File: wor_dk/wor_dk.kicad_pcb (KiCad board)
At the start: 4 copper layers, 135 parts, among them J101 Conn_01x02, J102 Conn_02x03_Odd_Even, J103 Conn_02x03_Odd_Even, J104 Conn_01x02, J201 SWD, J301 SMA, J302 Conn_02x04_Odd_Even, J303 Conn_02x06_Odd_Even, J401 USB_C_Receptacle_USB2.0_16P, J501 SWD, J502 USB_C_Receptacle_USB2.0_16P, J503 SWD, Q501 BSS84, SW201 SW_Push, SW501 SW_Push, U201 nRF52840, U202 TMUX1112PWR, U203 TMUX1112PWR, U301 Si4467, U401 FT232RL, U501 TLV1117-33, U502 LPC11U35FHI33_501, Y201 32.768kHz, Y202 32MHz, Y301 26MHz, Y501 12MHz

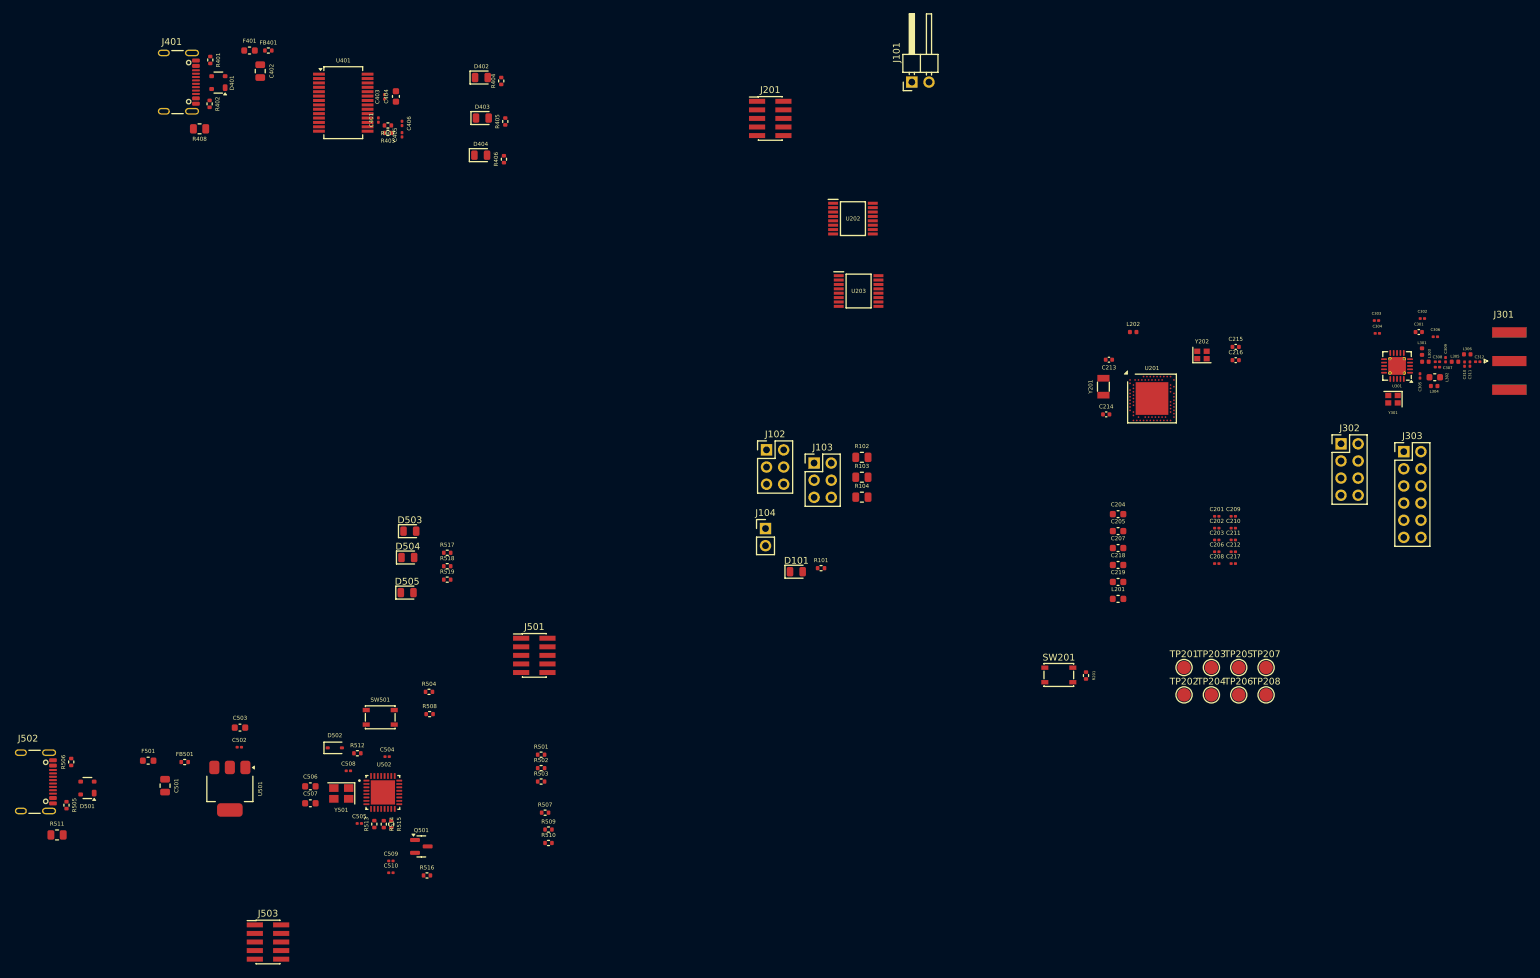
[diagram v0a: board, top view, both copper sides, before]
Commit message: wor_dk: PCB: finer parts placement & interface description
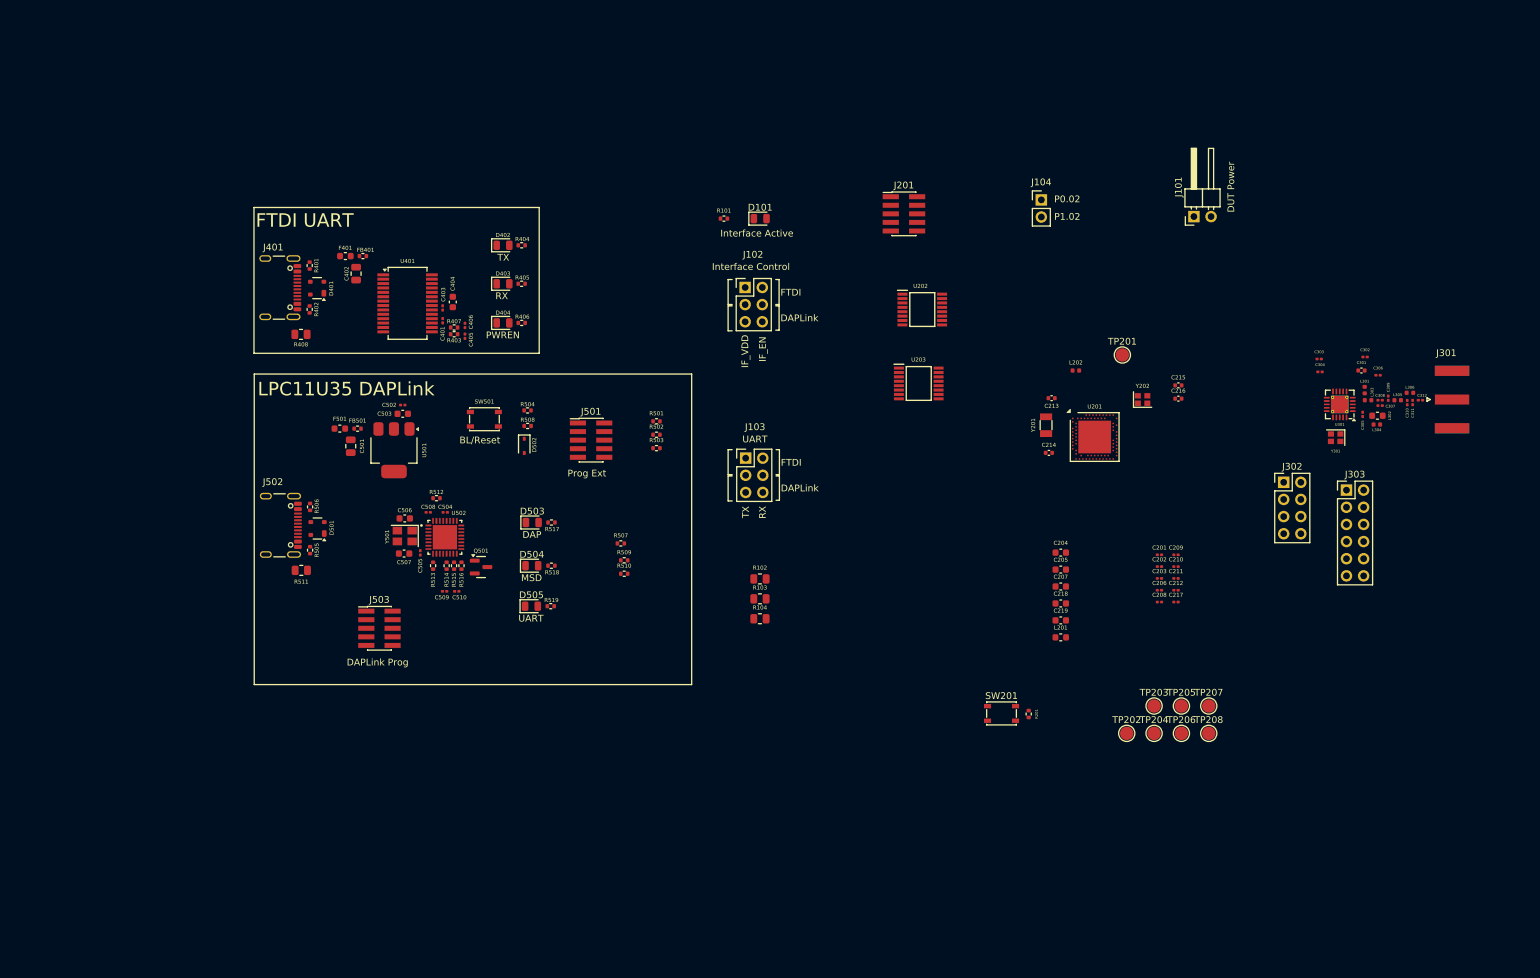
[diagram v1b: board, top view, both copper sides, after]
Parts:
- moved J104 63.6 mm to (172.8, 54.1)
- moved C501 57.3 mm to (70.5, 90.6)
- moved F501 56.8 mm to (68.9, 88.0)
- moved C502 56.2 mm to (78.2, 84.5)
- moved U501 55.7 mm to (76.9, 91.2)
- moved FB501 55.6 mm to (71.5, 88.0)
- moved R101 53.7 mm to (125.8, 56.9)
- moved R511 53.3 mm to (63.2, 109.0)
- moved D502 52.8 mm to (96.2, 90.6), turned to -90 degrees
- moved D101 52.6 mm to (131.2, 56.9)
- moved J502 52.5 mm to (59.0, 102.3)
- moved C503 52.4 mm to (78.2, 85.8)
- moved R501 52.3 mm to (115.8, 86.9)
- moved R502 52.3 mm to (115.8, 88.9)
- moved R503 52.3 mm to (115.8, 90.9)
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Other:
- board text added: "BL/Reset"
- board text added: "DAP"
- board text added: "DAPLink"
- board text added: "DAPLink Prog"
- board text added: "DUT Power"
- board text added: "FTDI"
- board text added: "FTDI UART"
- board text added: "IF_EN"
- board text added: "IF_VDD"
- board text added: "Interface Active"
- board text added: "Interface Control"
- board text added: "LPC11U35 DAPLink"
- board text added: "MSD"
- board text added: "P0.02"
- board text added: "P1.02"
- board text added: "PWREN"
- board text added: "Prog Ext"
- board text added: "RX"
- board text added: "TX"
- board text added: "UART"

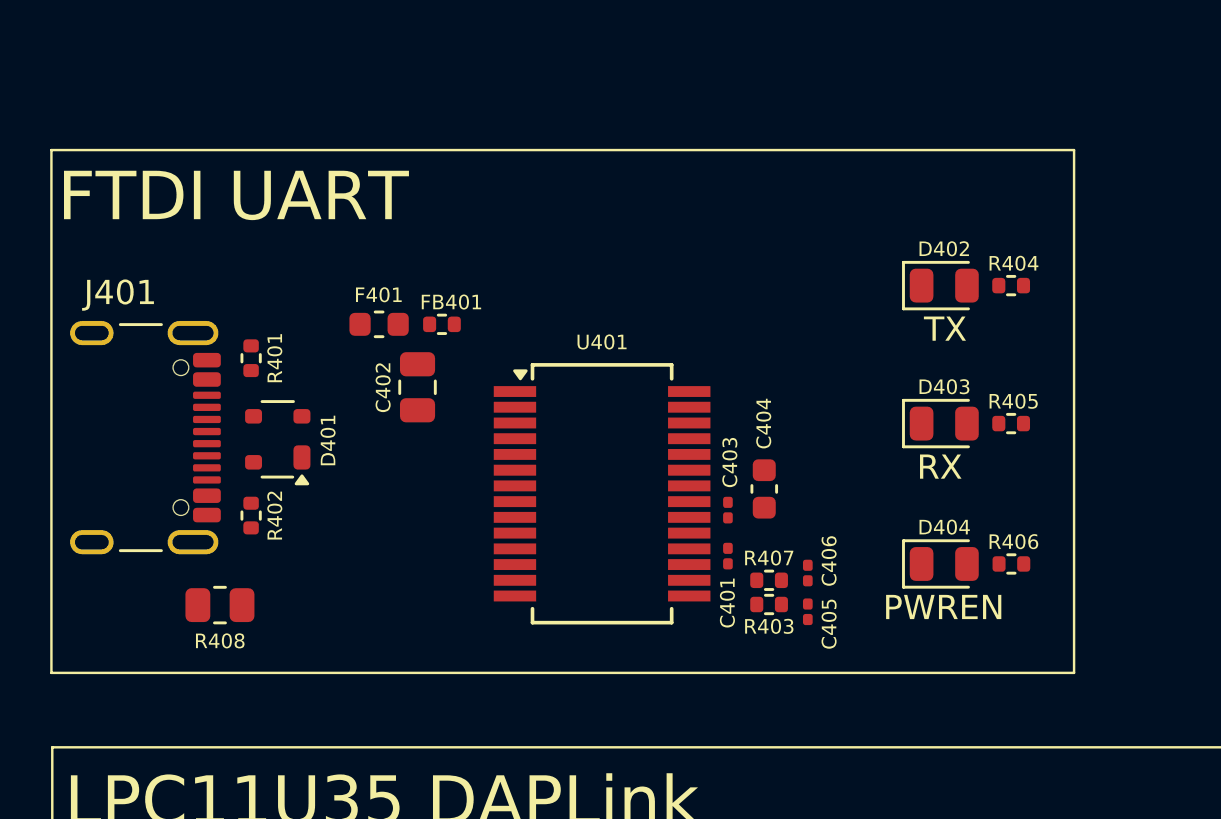
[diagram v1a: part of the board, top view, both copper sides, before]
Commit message: wor_dk: PCB: routing for FTDI part
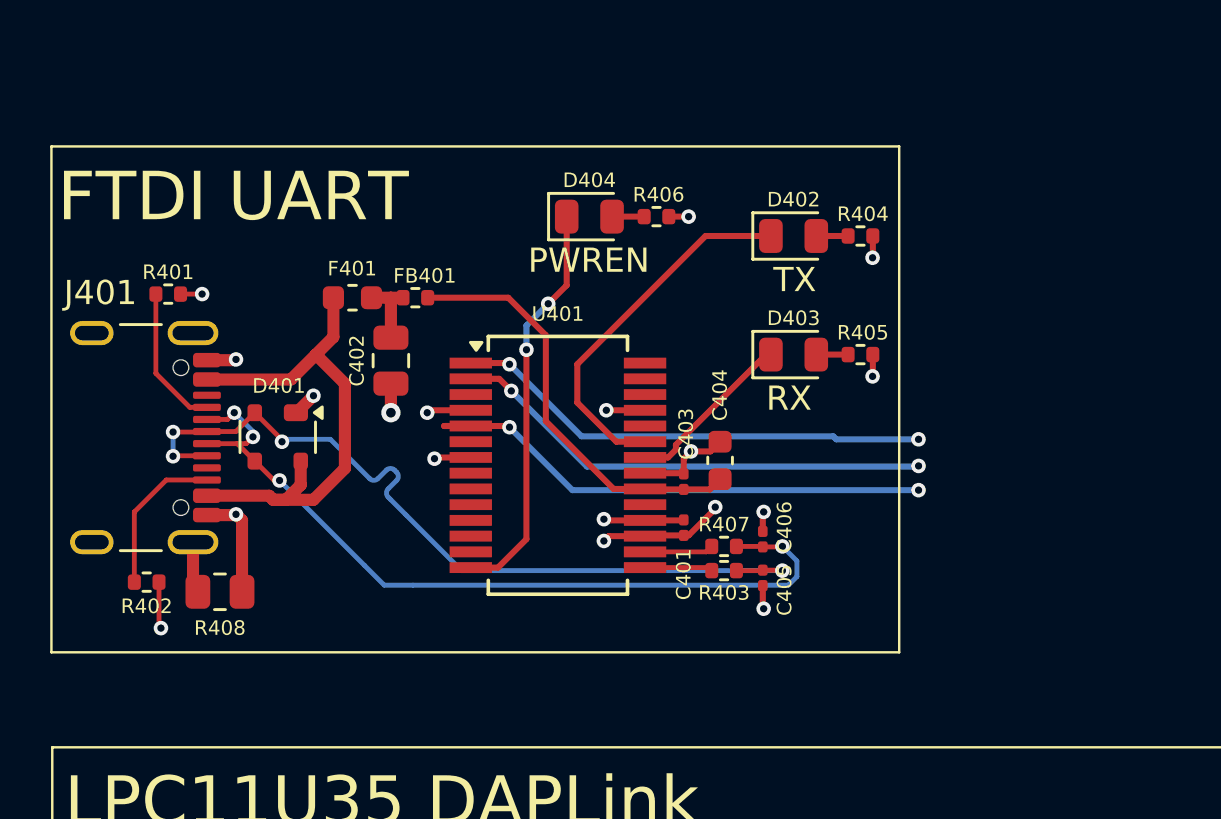
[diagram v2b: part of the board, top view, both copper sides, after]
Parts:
- moved D404 20.5 mm to (78.4, 58.0)
- moved R406 20.5 mm to (81.2, 58.0)
- moved R405 6.85 mm to (89.6, 63.7)
- moved D403 6.85 mm to (86.8, 63.7)
- moved R404 6.55 mm to (89.6, 58.8)
- moved D402 6.55 mm to (86.8, 58.8)
- moved R402 5.12 mm to (60.1, 73.1), turned to 0 degrees
- moved R401 4.33 mm to (61.0, 61.2), turned to 180 degrees
- moved C405 2.33 mm to (85.6, 72.9)
- moved R403 2.33 mm to (84.0, 72.6)
- moved R407 2.33 mm to (84.0, 71.6)
- moved C406 2.33 mm to (85.6, 71.3)
- moved C401 2.17 mm to (82.3, 70.8)
- moved C403 2.17 mm to (82.3, 69.0)
- moved C404 2.17 mm to (83.8, 68.1)
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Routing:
- net /FT232R/USB_D+: track 0.00 -> 34.2 mm, vias 0 -> 4
- net /FT232R/USB_D-: track 0.00 -> 33.7 mm, vias 0 -> 4
- net GND: track 0.00 -> 23.0 mm, vias 0 -> 12
- net /RXD_FTDI: track 0.00 -> 21.8 mm, vias 0 -> 2
- net /FT232R/VBUS: track 0.00 -> 21.5 mm
- net /DTR_FTDI: track 0.00 -> 20.0 mm, vias 0 -> 2
- net /TXD_FTDI: track 0.00 -> 19.8 mm, vias 0 -> 2
- net Net-(U401-VCC): track 0.00 -> 17.6 mm
- net Net-(D404-K): track 0.00 -> 16.8 mm, vias 0 -> 2
- net Net-(D402-K): track 0.00 -> 15.2 mm
- net /3V3_FTDI: track 0.00 -> 9.69 mm, vias 0 -> 6
- net Net-(D403-K): track 0.00 -> 7.08 mm
- net Net-(J401-CC2): track 0.00 -> 6.45 mm
- net Net-(J401-CC1): track 0.00 -> 5.97 mm
- net Net-(C402-Pad1): track 0.00 -> 2.95 mm
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- added copper zone on In2.Cu, net /3V3_FTDI
- added copper zone on In1.Cu, net GND

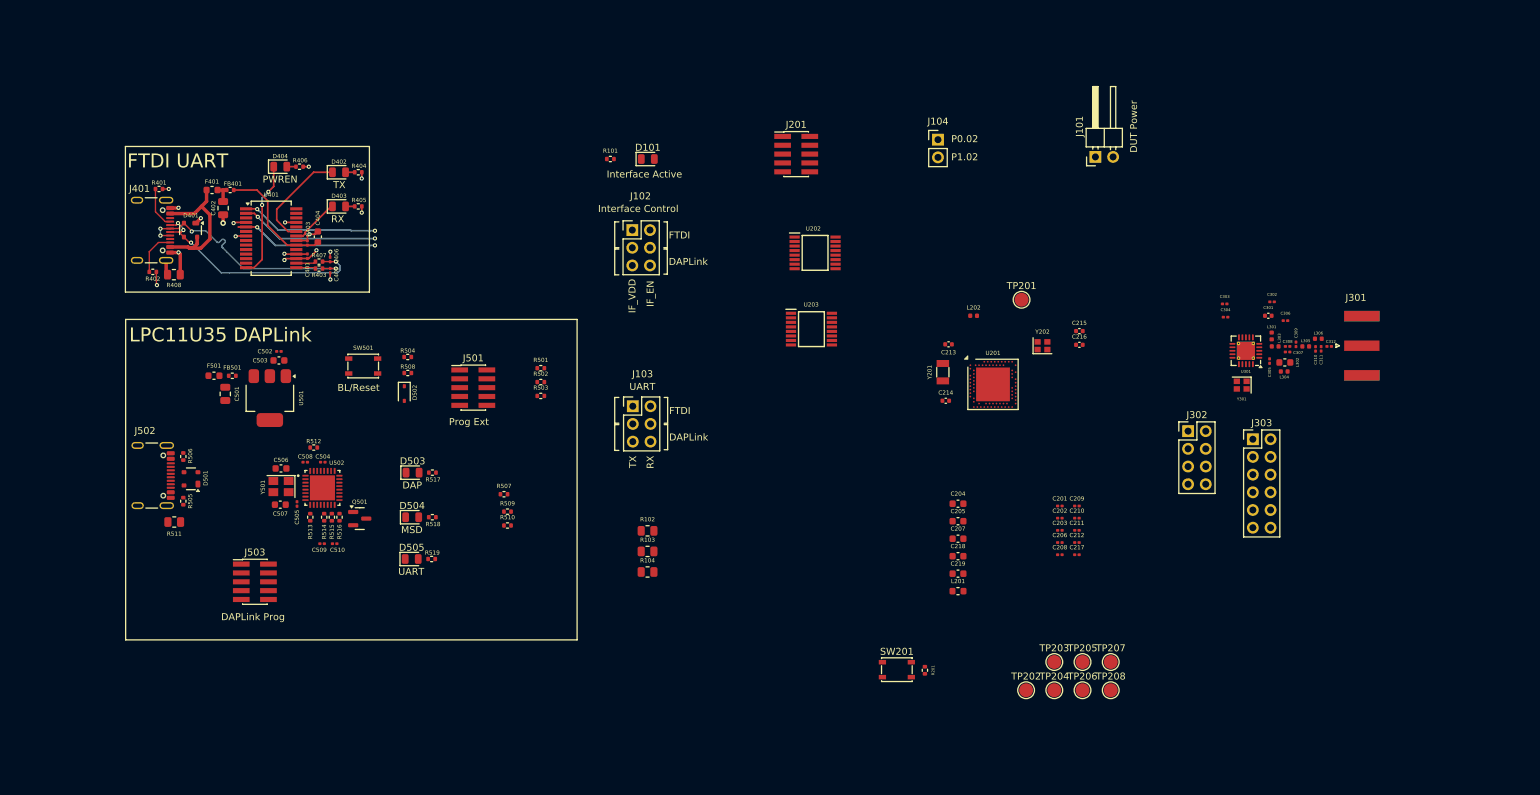
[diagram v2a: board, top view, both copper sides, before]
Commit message: wor_dk: PCB: routing for LPC11U35 DAPLink
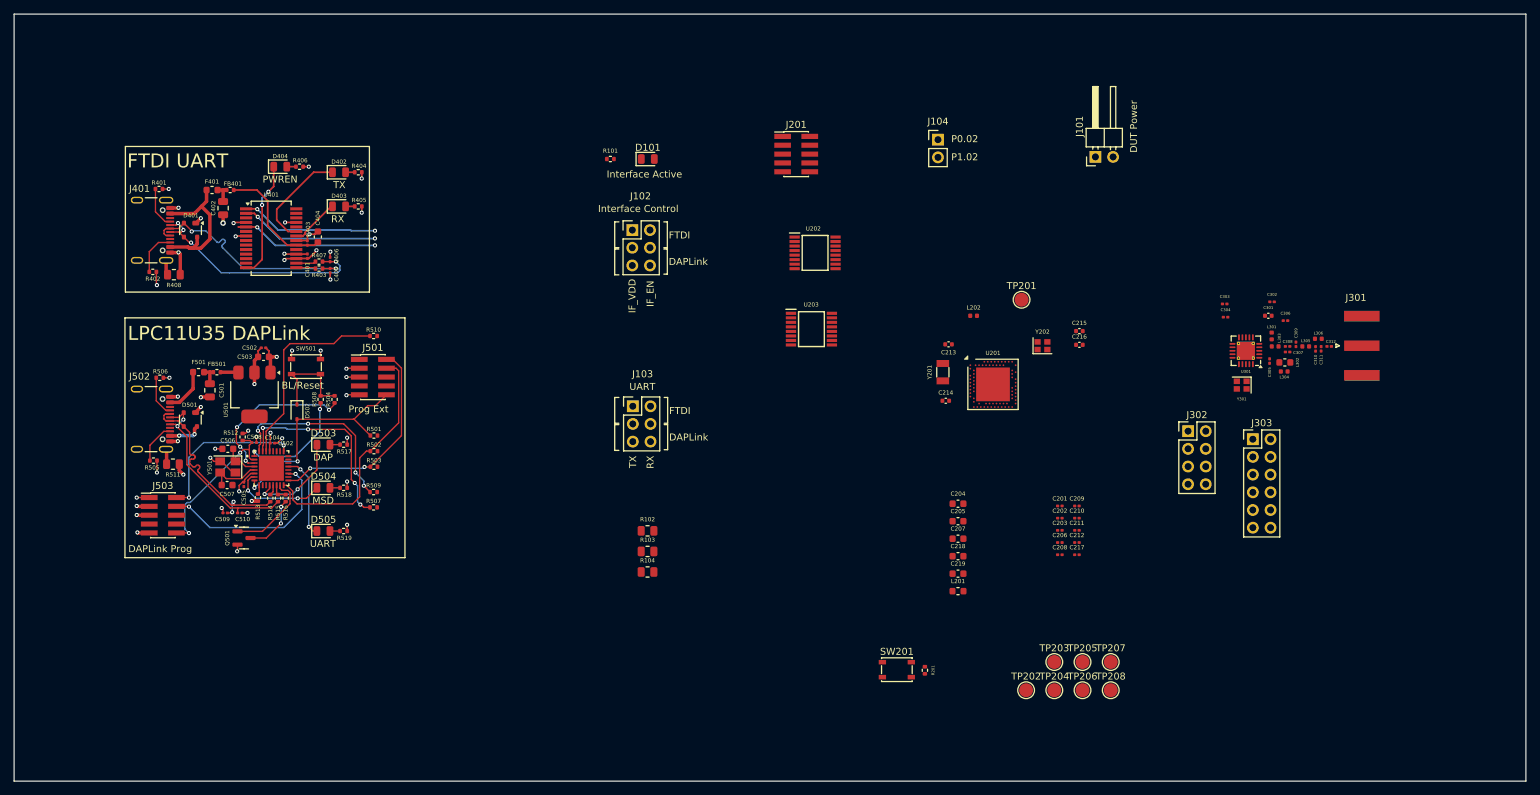
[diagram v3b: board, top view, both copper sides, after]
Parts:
- moved R510 33.3 mm to (91.8, 82.3)
- moved R503 26.0 mm to (91.8, 101.1)
- moved R502 25.9 mm to (91.8, 98.8)
- moved R501 25.8 mm to (91.8, 96.6)
- moved R509 19.4 mm to (91.8, 104.7)
- moved R507 18.8 mm to (91.8, 106.9)
- moved Q501 16.8 mm to (73.2, 111.3)
- moved J503 16.3 mm to (61.5, 108.0)
- moved D502 15.6 mm to (80.8, 93.2)
- moved C509 14.6 mm to (70.5, 107.7)
- moved J501 14.5 mm to (91.7, 88.2)
- moved C510 14.3 mm to (72.6, 107.7)
- moved D504 13.4 mm to (84.6, 104.1)
- moved R518 13.4 mm to (87.5, 104.1)
- moved D503 13.4 mm to (84.6, 97.9)
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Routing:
- net GND: track 23.0 -> 60.1 mm, vias 12 -> 34
- net /LPC11U35 DAPLink Programmer/TGT_SWCLK: track 0.00 -> 35.8 mm
- net /LPC11U35 DAPLink Programmer/TGT_NRESET: track 0.00 -> 32.5 mm, vias 0 -> 2
- net /LPC11U35 DAPLink Programmer/TGT_SWDIO: track 0.00 -> 31.3 mm, vias 0 -> 2
- net /LPC11U35 DAPLink Programmer/USB_D-: track 0.00 -> 29.6 mm, vias 0 -> 2
- net /DTR_DAP: track 0.00 -> 28.8 mm
- net /LPC11U35 DAPLink Programmer/USB_D+: track 0.00 -> 28.6 mm, vias 0 -> 2
- net /RXD_DAP: track 0.00 -> 28.5 mm, vias 0 -> 4
- net /TXD_DAP: track 0.00 -> 27.6 mm, vias 0 -> 4
- net /LPC11U35 DAPLink Programmer/IF_SWCLK: track 0.00 -> 26.9 mm, vias 0 -> 2
- net /LPC11U35 DAPLink Programmer/IF_NRESET: track 0.00 -> 23.3 mm, vias 0 -> 2
- net /LPC11U35 DAPLink Programmer/IF_SWDIO: track 0.00 -> 23.1 mm, vias 0 -> 2
- net /LPC11U35 DAPLink Programmer/TGT_NRESET_FB: track 0.00 -> 22.9 mm, vias 0 -> 4
- net VDD_PROG: track 0.00 -> 19.7 mm, vias 0 -> 10
- net /LPC11U35 DAPLink Programmer/TGT_NRESET_FB_ISP: track 0.00 -> 16.0 mm, vias 0 -> 2
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- added copper zone on In2.Cu, net VDD_PROG
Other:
- board outline added: 217 x 110.1 mm
